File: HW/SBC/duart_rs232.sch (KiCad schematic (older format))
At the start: 11 parts, among them J6 RS232a, J7 RS232b, U22 MAX238, U23 SC28L92PLCC44, X2 3.6864MHz

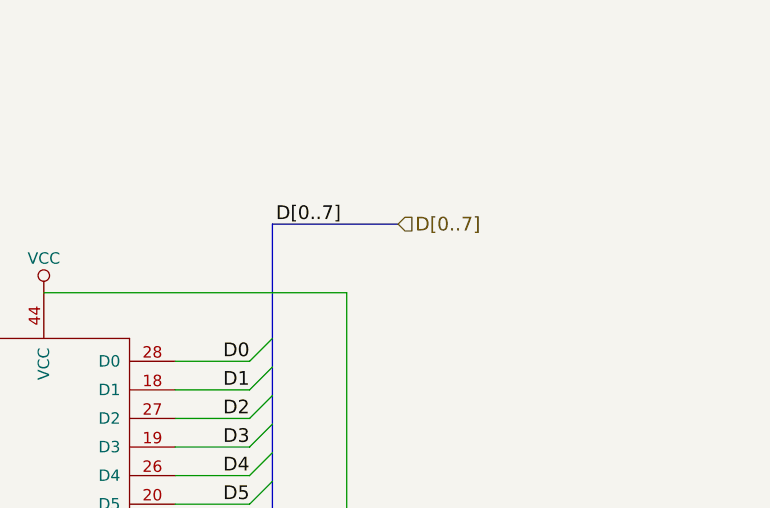
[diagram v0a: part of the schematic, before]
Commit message: Added CPLD to schematics. Updates rest of schematics to use CPLD
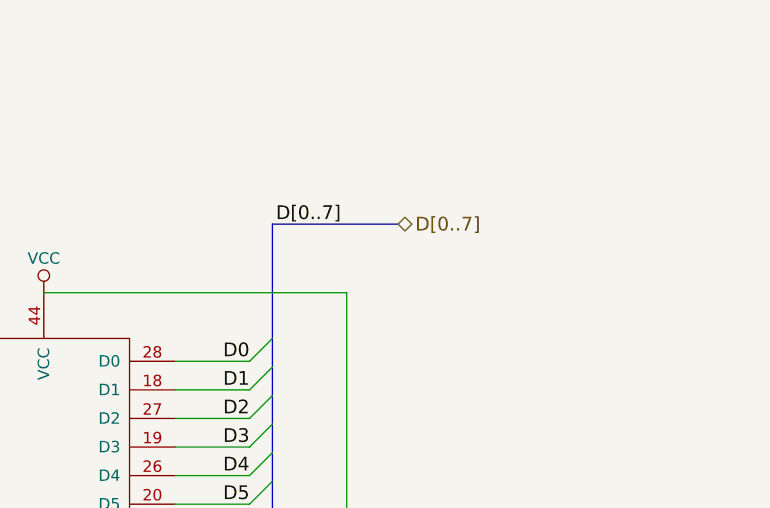
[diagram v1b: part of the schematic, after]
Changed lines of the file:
@@
 $Descr A4 11693 8268
 encoding utf-8
-Sheet 8 8
+Sheet 7 7
 Title ""
 Date ""
@@
 $EndComp
 $Comp
-L GND #PWR054
+L GND #PWR047
 U 1 1 59ECE27A
 P 2750 1875
-F 0 "#PWR054" H 2750 1625 50  0001 C CNN
+F 0 "#PWR047" H 2750 1625 50  0001 C CNN
 F 1 "GND" H 2750 1725 50  0000 C CNN
 F 2 "" H 2750 1875 50  0001 C CNN
@@
 $EndComp
 $Comp
-L VCC #PWR055
+L VCC #PWR048
 U 1 1 59ECE2B2
 P 3675 1075
-F 0 "#PWR055" H 3675 925 50  0001 C CNN
+F 0 "#PWR048" H 3675 925 50  0001 C CNN
 F 1 "VCC" H 3675 1225 50  0000 C CNN
 F 2 "" H 3675 1075 50  0001 C CNN
@@
 $EndComp
 $Comp
-L GND #PWR056
+L GND #PWR049
 U 1 1 59ECE354
 P 4650 1150
-F 0 "#PWR056" H 4650 900 50  0001 C CNN
+F 0 "#PWR049" H 4650 900 50  0001 C CNN
 F 1 "GND" V 4650 975 50  0000 C CNN
 F 2 "" H 4650 1150 50  0001 C CNN
@@
 Text Label 8375 1775 2    60   ~ 0
 D[0..7]
-Text HLabel 8625 1775 2    60   Input ~ 0
+Text HLabel 8625 1775 2    60   BiDi ~ 0
 D[0..7]
 $Comp
-L GND #PWR057
+L GND #PWR050
 U 1 1 59ED2D15
 P 7075 5525
-F 0 "#PWR057" H 7075 5275 50  0001 C CNN
+F 0 "#PWR050" H 7075 5275 50  0001 C CNN
 F 1 "GND" H 7075 5375 50  0000 C CNN
 F 2 "" H 7075 5525 50  0001 C CNN
@@
 $EndComp
 $Comp
-L VCC #PWR058
+L VCC #PWR051
 U 1 1 59ED2EFD
 P 7075 2075
-F 0 "#PWR058" H 7075 1925 50  0001 C CNN
+F 0 "#PWR051" H 7075 1925 50  0001 C CNN
 F 1 "VCC" H 7075 2225 50  0000 C CNN
 F 2 "" H 7075 2075 50  0001 C CNN
@@
 RTSa
 $Comp
-L GND #PWR059
+L GND #PWR052
 U 1 1 59ED763B
 P 3675 4150
-F 0 "#PWR059" H 3675 3900 50  0001 C CNN
+F 0 "#PWR052" H 3675 3900 50  0001 C CNN
 F 1 "GND" H 3675 4000 50  0000 C CNN
 F 2 "" H 3675 4150 50  0001 C CNN
@@
 $EndComp
 $Comp
-L VCC #PWR060
+L VCC #PWR053
 U 1 1 59EE01CB
 P 9675 4575
-F 0 "#PWR060" H 9675 4425 50  0001 C CNN
+F 0 "#PWR053" H 9675 4425 50  0001 C CNN
 F 1 "VCC" H 9675 4725 50  0000 C CNN
 F 2 "" H 9675 4575 50  0001 C CNN
@@
 $EndComp
 $Comp
-L GND #PWR061
+L GND #PWR054
 U 1 1 59EE022C
 P 9675 5175
-F 0 "#PWR061" H 9675 4925 50  0001 C CNN
+F 0 "#PWR054" H 9675 4925 50  0001 C CNN
 F 1 "GND" H 9675 5025 50  0000 C CNN
 F 2 "" H 9675 5175 50  0001 C CNN
@@
 	9375 4875 7650 4875
 $Comp
-L VCC #PWR062
+L VCC #PWR055
 U 1 1 59EE05A1
 P 8575 5125
-F 0 "#PWR062" H 8575 4975 50  0001 C CNN
+F 0 "#PWR055" H 8575 4975 50  0001 C CNN
 F 1 "VCC" V 8575 5300 50  0000 C CNN
 F 2 "" H 8575 5125 50  0001 C CNN
@@
 	900  2750 900  3050
 $Comp
-L GND #PWR063
+L GND #PWR056
 U 1 1 59F06F3D
 P 900 3050
-F 0 "#PWR063" H 900 2800 50  0001 C CNN
+F 0 "#PWR056" H 900 2800 50  0001 C CNN
 F 1 "GND" H 900 2900 50  0000 C CNN
 F 2 "" H 900 3050 50  0001 C CNN
@@
 $EndComp
 $Comp
-L GND #PWR064
+L GND #PWR057
 U 1 1 59F06F91
 P 900 3775
-F 0 "#PWR064" H 900 3525 50  0001 C CNN
+F 0 "#PWR057" H 900 3525 50  0001 C CNN
 F 1 "GND" H 900 3625 50  0000 C CNN
 F 2 "" H 900 3775 50  0001 C CNN
